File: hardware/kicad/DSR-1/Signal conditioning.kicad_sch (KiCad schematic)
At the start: 0 parts

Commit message: Completed microcontroller schematic
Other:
- title: (none) -> Signal Conditioning
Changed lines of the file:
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@@
 	(generator_version "10.0")
 	(paper "A4")
+	(title_block
+		(title "Signal Conditioning")
+		(date "2026-05-31")
+		(rev "1")
+	)
 	(hierarchical_label "FG_IN"
 		(shape output)

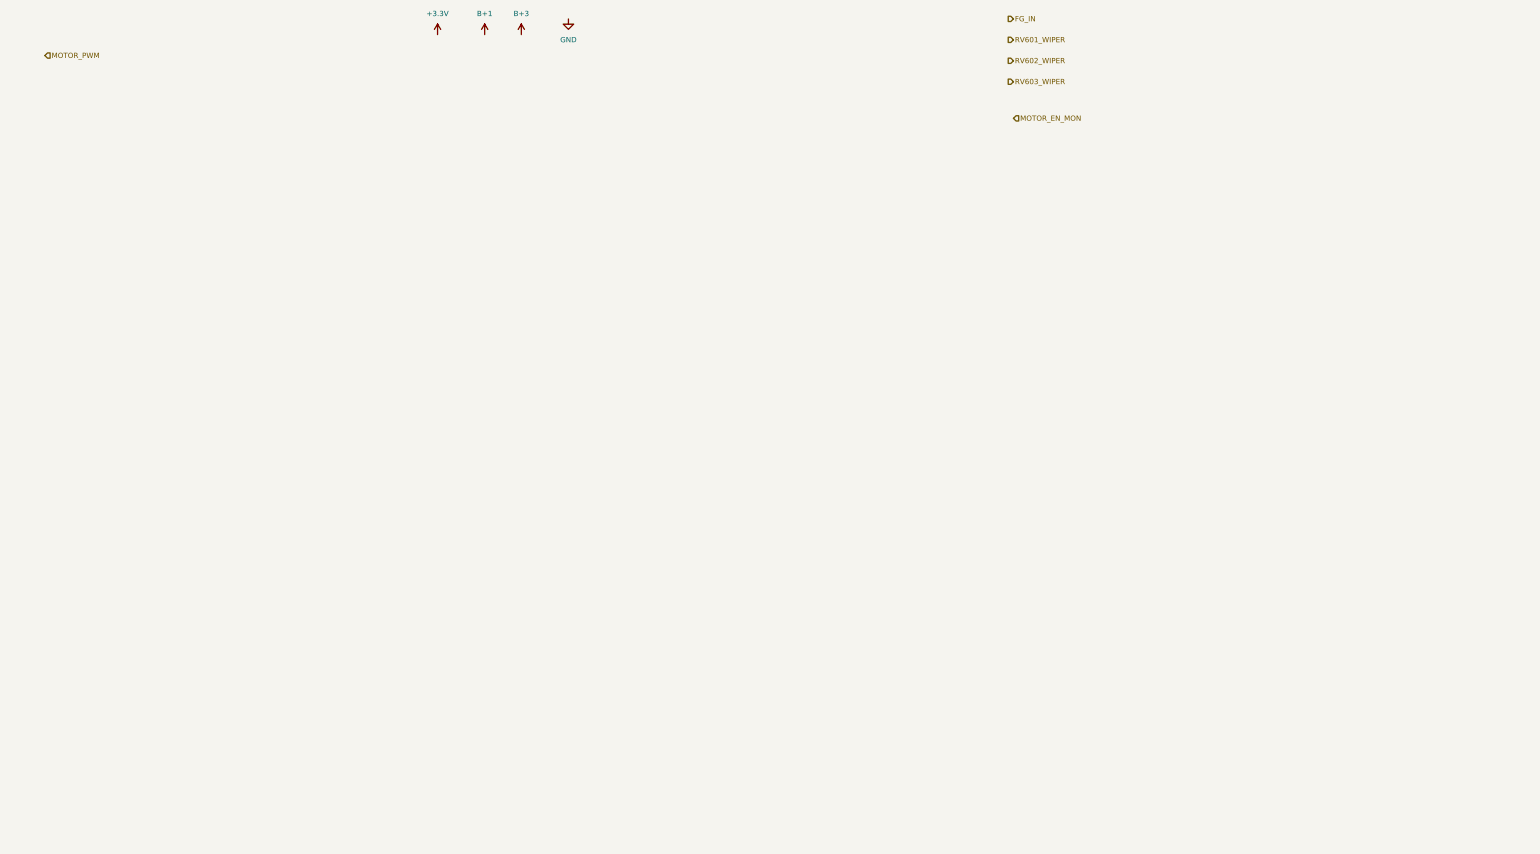
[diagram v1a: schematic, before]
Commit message: completed schematics through sheet 5.
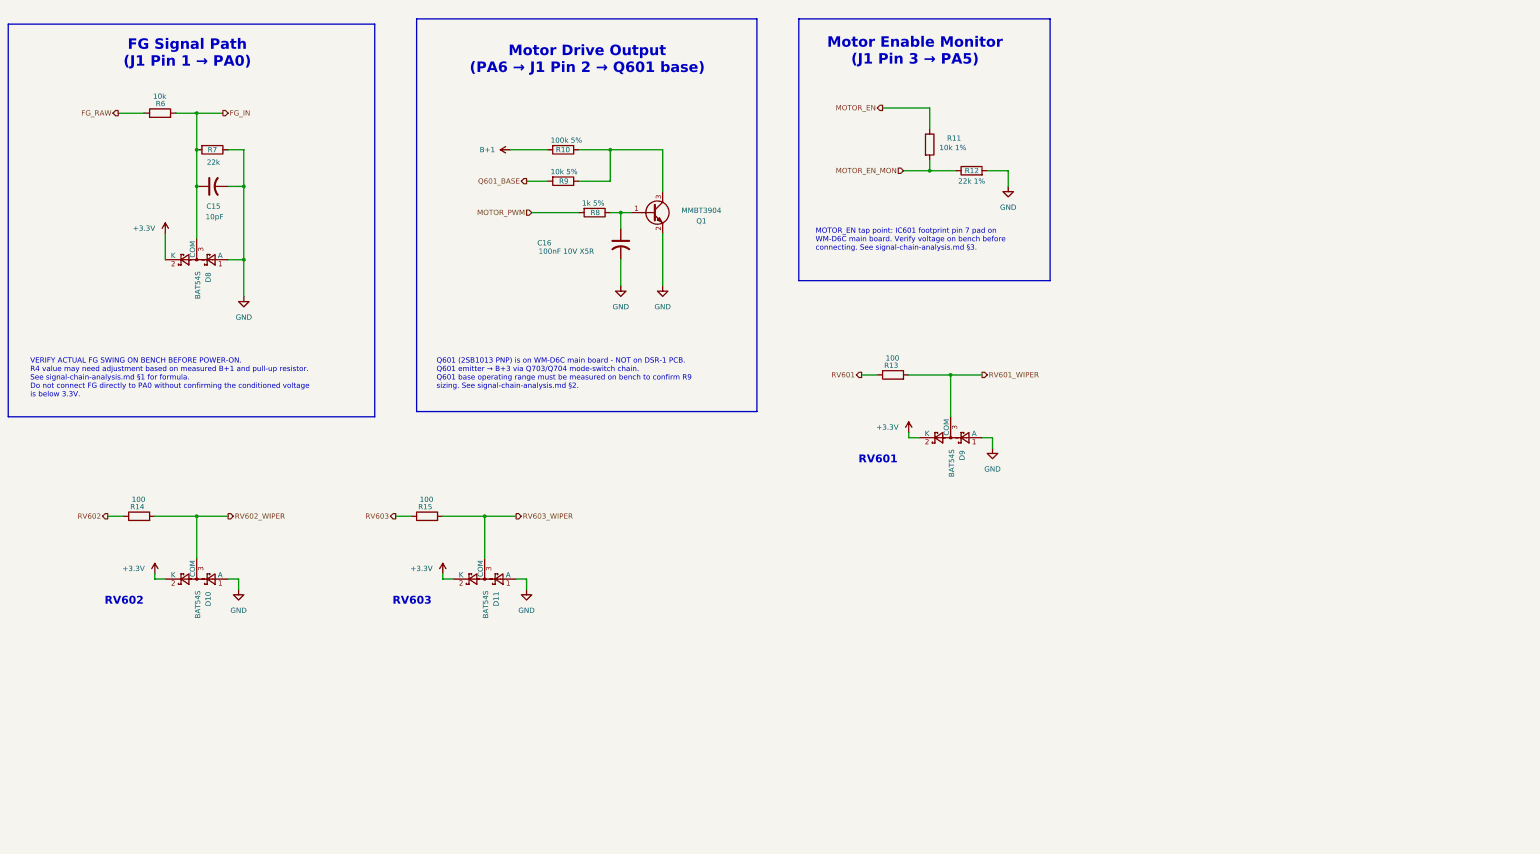
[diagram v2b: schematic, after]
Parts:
- added C15: 10pF, symbol Device:C_US
- added C16: 100nF 10V X5R, symbol Device:C_US
- added D10, D11, D8, D9: BAT54S, Package_TO_SOT_SMD:SOT-23, symbol DSR-1:BAT54S
- added Q1: MMBT3904, Package_TO_SOT_SMD:SOT-23, symbol DSR-1:MMBT3904
- added R10: 100k 5%, symbol Device:R
- added R11: 10k 1%, symbol Device:R
- added R12: 22k 1%, symbol Device:R
- added R13, R14, R15: 100, symbol Device:R
- added R6: 10k, symbol Device:R
- added R7: 22k, symbol Device:R
- added R8: 1k 5%, symbol Device:R
- added R9: 10k 5%, symbol Device:R
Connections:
- net +3.3V: now also D10.2 (K), D11.2 (K), D8.2 (K), D9.2 (K)
- net B+1: now also R10.2
- net FG_IN: now also C15.1, D8.3 (COM), R6.2, R7.2
- net GND: now also C15.2, C16.2, D10.1 (A), D11.1 (A), D8.1 (A), D9.1 (A), Q1.2 (E), R12.2, R7.1
- net MOTOR_EN_MON: now also R11.2, R12.1
- net MOTOR_PWM: now also R8.2
- net RV601_WIPER: now also D9.3 (COM), R13.2
- net RV602_WIPER: now also D10.3 (COM), R14.2
- net RV603_WIPER: now also D11.3 (COM), R15.2
- new net: C16.1, Q1.1 (B), R8.1
- new net: Q1.3 (C), R10.1, R9.1
- new net FG_RAW: R6.1
- new net MOTOR_EN: R11.1
- new net Q601_BASE: R9.2
- new net RV601: R13.1
- new net RV602: R14.1
- new net RV603: R15.1
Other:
- note added: "FG Signal Path (J1 Pin 1 → PA0)"
- note added: "MOTOR_EN tap point: IC601 footprint pin 7 pad on WM-D6C main board. Verify voltage on bench before connecting. See signal-chain-analysis.md §3."
- note added: "Motor Drive Output (PA6 → J1 Pin 2 → Q601 base)"
- note added: "Motor Enable Monitor (J1 Pin 3 → PA5)"
- note added: "Q601 (2SB1013 PNP) is on WM-D6C main board - NOT on DSR-1 PCB. Q601 emitter → B+3 via Q703/Q704 mode-switch chain. Q601 base operating range must be measured on bench to confirm R9 sizing. See signal-chain-analysis.md §2."
- note added: "RV601"
- note added: "RV602"
- note added: "RV603"
- note added: "VERIFY ACTUAL FG SWING ON BENCH BEFORE POWER-ON. R4 value may need adjustment based on measured B+1 and pull-up resistor. See signal-chain-analysis.md §1 for formula. Do not connect FG directly to PA0 without confirming the conditioned voltage is below 3.3V."

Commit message: Adjusted visual layout of sheet 5
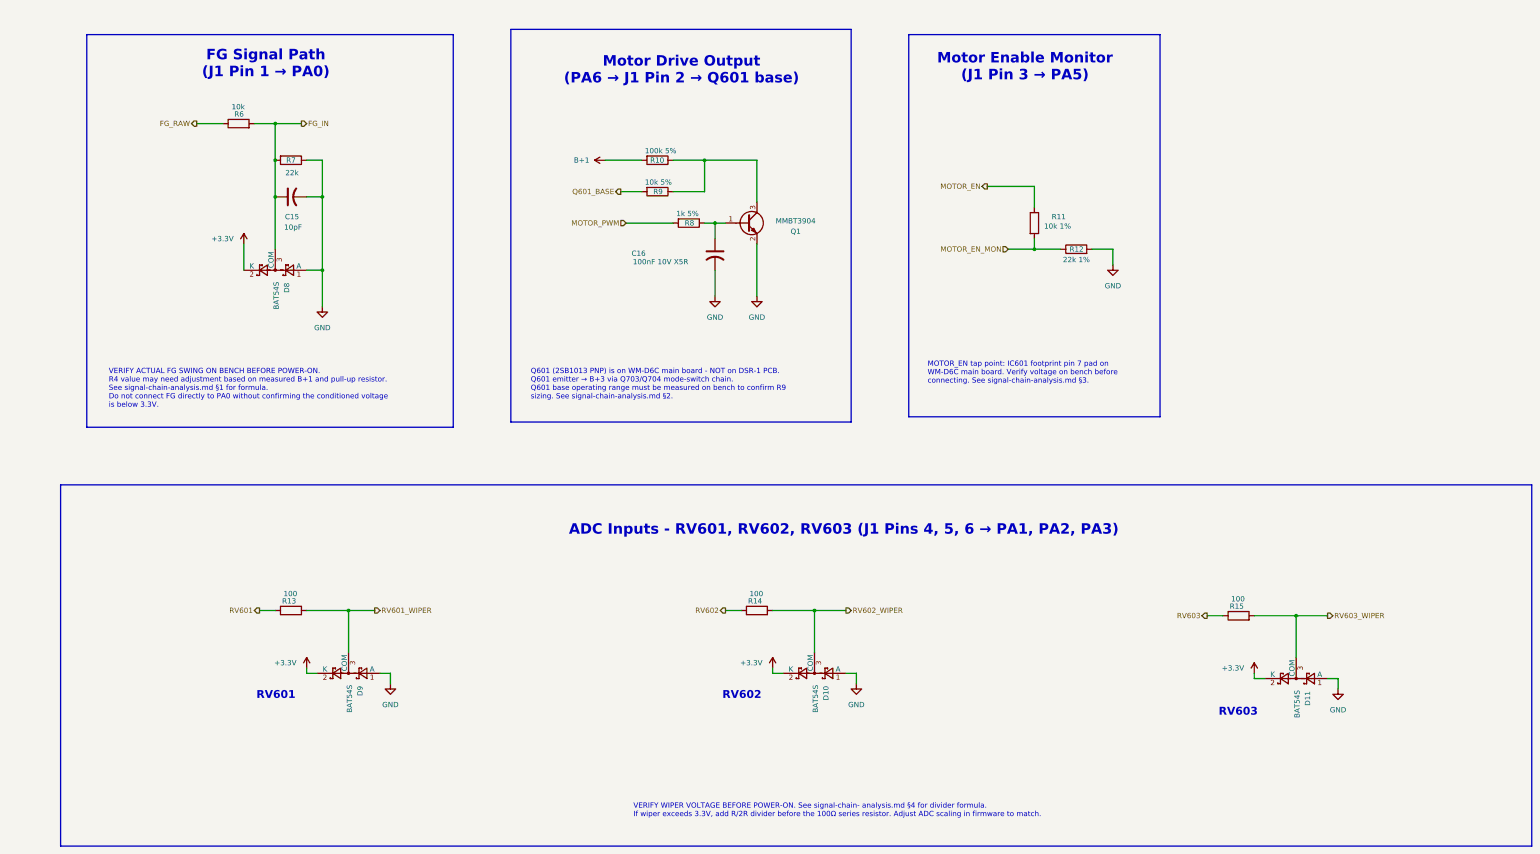
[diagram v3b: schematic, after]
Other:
- note added: "ADC Inputs - RV601, RV602, RV603 (J1 Pins 4, 5, 6 → PA1, PA2, PA3)"
- note added: "VERIFY WIPER VOLTAGE BEFORE POWER-ON. See signal-chain- analysis.md §4 for divider formula. If wiper exceeds 3.3V, add R/2R divider before the 100Ω series resistor. Adjust ADC scaling in firmware to match."
- moved on the sheet: C15, C16, D10, D11, D8, D9, Q1, R10, R11, R12, R13, R14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
